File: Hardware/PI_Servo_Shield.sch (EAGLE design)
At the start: 58 parts, among them J1 RASPBERRYPI-40-PIN-GPIO, J19 QWIIC, J20 USB C, J21 Serial, U1 PCA9685, U2 PCA9306, U3 CH340C

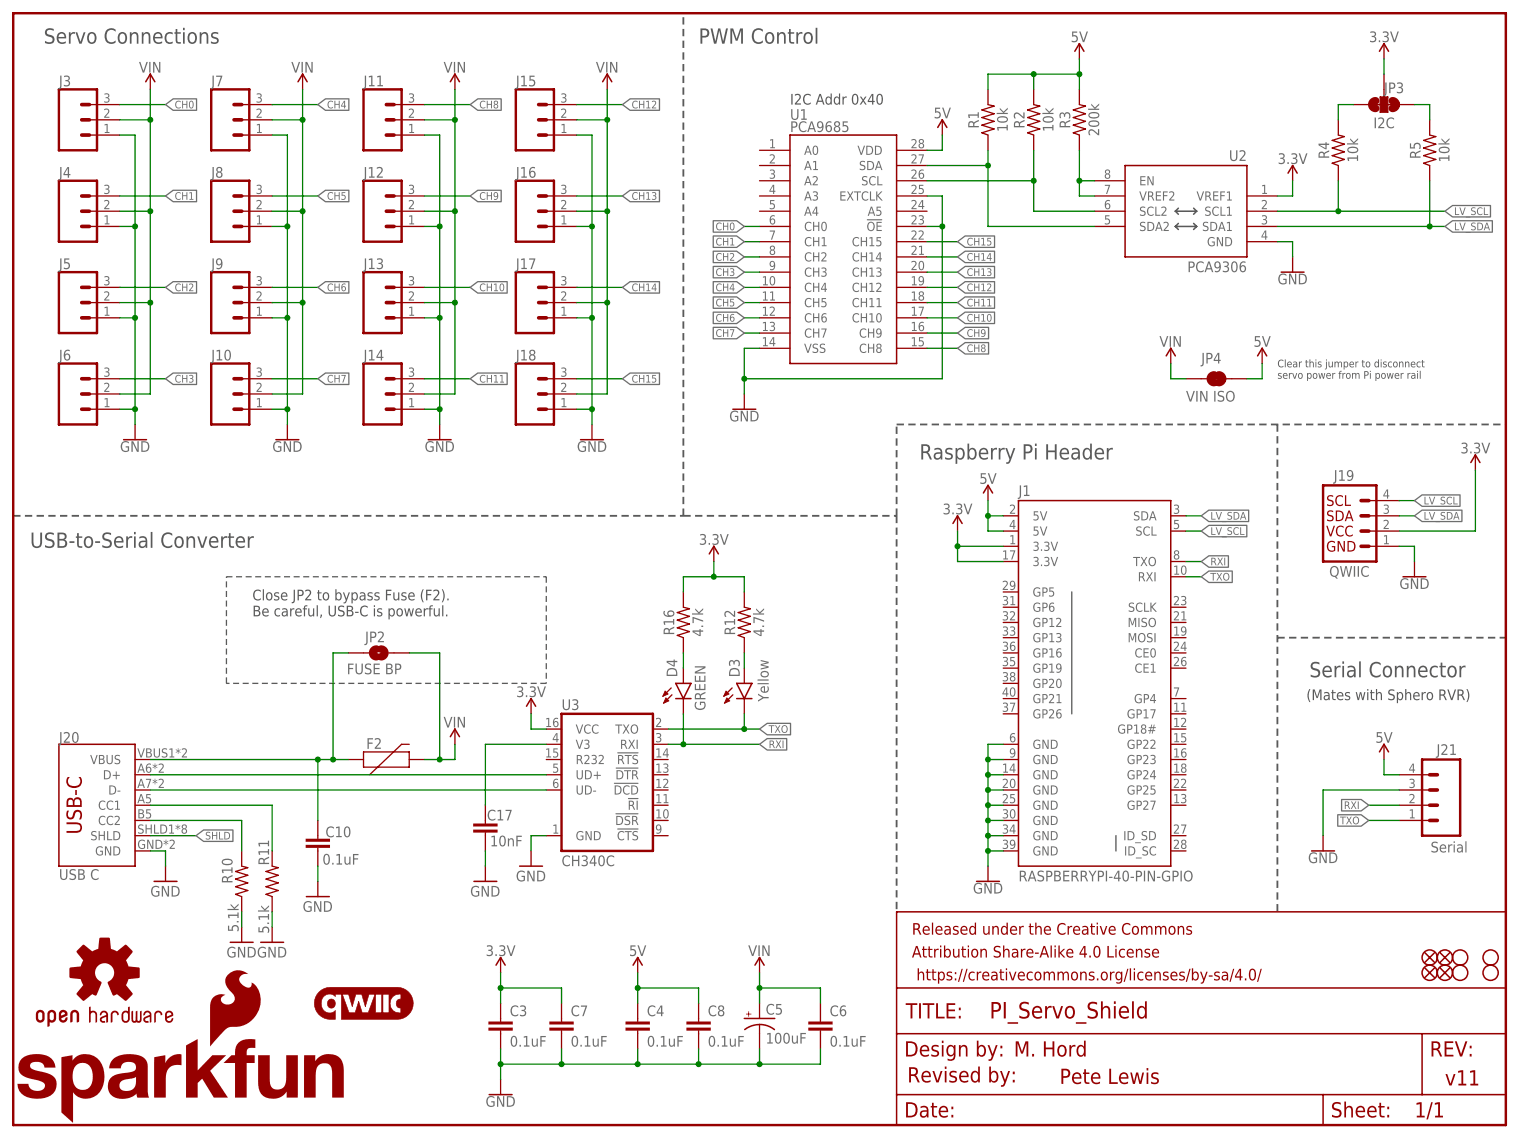
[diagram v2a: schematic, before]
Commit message: post checklist changes - silk and testpoints
-silk outlines up to 8 mil on a few.
-testpoints
-RX/TX LED colors corrected
-some PROD_ID stuff fixed.
-text note in sch for i2c jumper
-voltage warning for > +5V RVR input damaging pi.
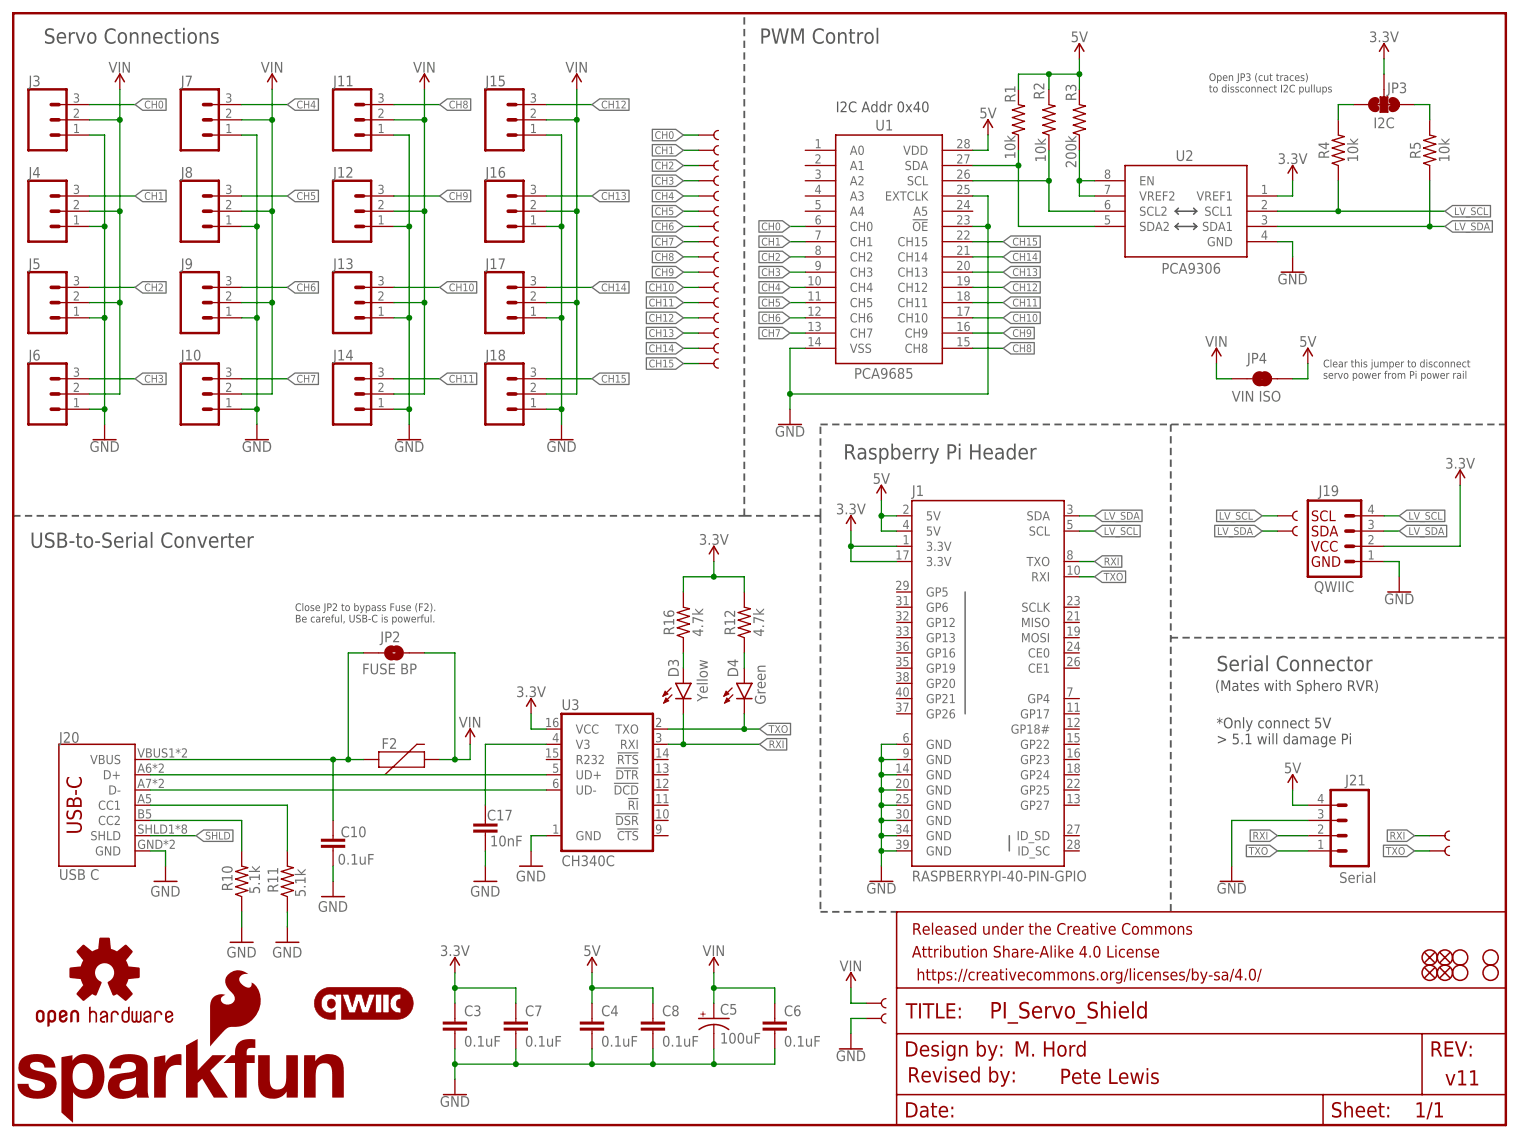
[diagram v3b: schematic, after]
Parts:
- added TP0, TP1, TP10, TP11, TP12, TP13, TP14, TP15, TP16, TP17, TP2, TP20, TP21, TP3, TP4, TP5, TP6, TP7, TP8, TP9: TEST-POINT3X4, SparkFun-Connectors:TEST-POINT3X4
- added TP18, TP19: TEST-POINTTP_15TH_THRU, SparkFun-Connectors:TEST-POINTTP_15TH_THRU
- C3, C4, C6, C7, C8: device SparkFun-Capacitors:0.1UF-0603-25V-5% -> SparkFun-Capacitors:0.1UF-0603-25V-(+80/-20%)
- D3: device SparkFun-LED:LED-YELLOW_HIDDENSILK -> SparkFun-LED:LED-GREEN_HIDDENSILK
- D4: device SparkFun-LED:LED-GREENLILYPAD -> SparkFun-LED:LED-YELLOW_HIDDENSILK
- J20: device USB-C:USB_C16PIN -> SparkFun-Connectors:USB_C16PIN
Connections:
- removed net N$12: D4.A, R16.1
- removed net N$13: D3.A, R12.1
- new net N$6: D3.A, R16.1
- new net N$7: D4.A, R12.1
- net CH0: now also TP0.1
- net CH1: now also TP1.1
- net CH10: now also TP10.1
- net CH11: now also TP11.1
- net CH12: now also TP12.1
- net CH13: now also TP13.1
- net CH14: now also TP14.1
- net CH15: now also TP15.1
- net CH2: now also TP2.1
- net CH3: now also TP3.1
- net CH4: now also TP4.1
- net CH5: now also TP5.1
- net CH6: now also TP6.1
- net CH7: now also TP7.1
- net CH8: now also TP8.1
- net CH9: now also TP9.1
- net GND: now also TP17.1
- net LV_SCL: now also TP18.1
- net LV_SDA: now also TP19.1
- net RXI: now also D3.C, TP20.1; no longer D4.C
- net TXO: now also D4.C, TP21.1; no longer D3.C
- net VIN: now also TP16.1
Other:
- note added: "*Only connect 5V > 5.1 will damage Pi"
- note added: "Green"
- note added: "Open JP3 (cut traces) to dissconnect I2C pullups"
- moved on the sheet: C10, C3, C4, C5, C6, C7, C8, D3, D4, F2, J1, J10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

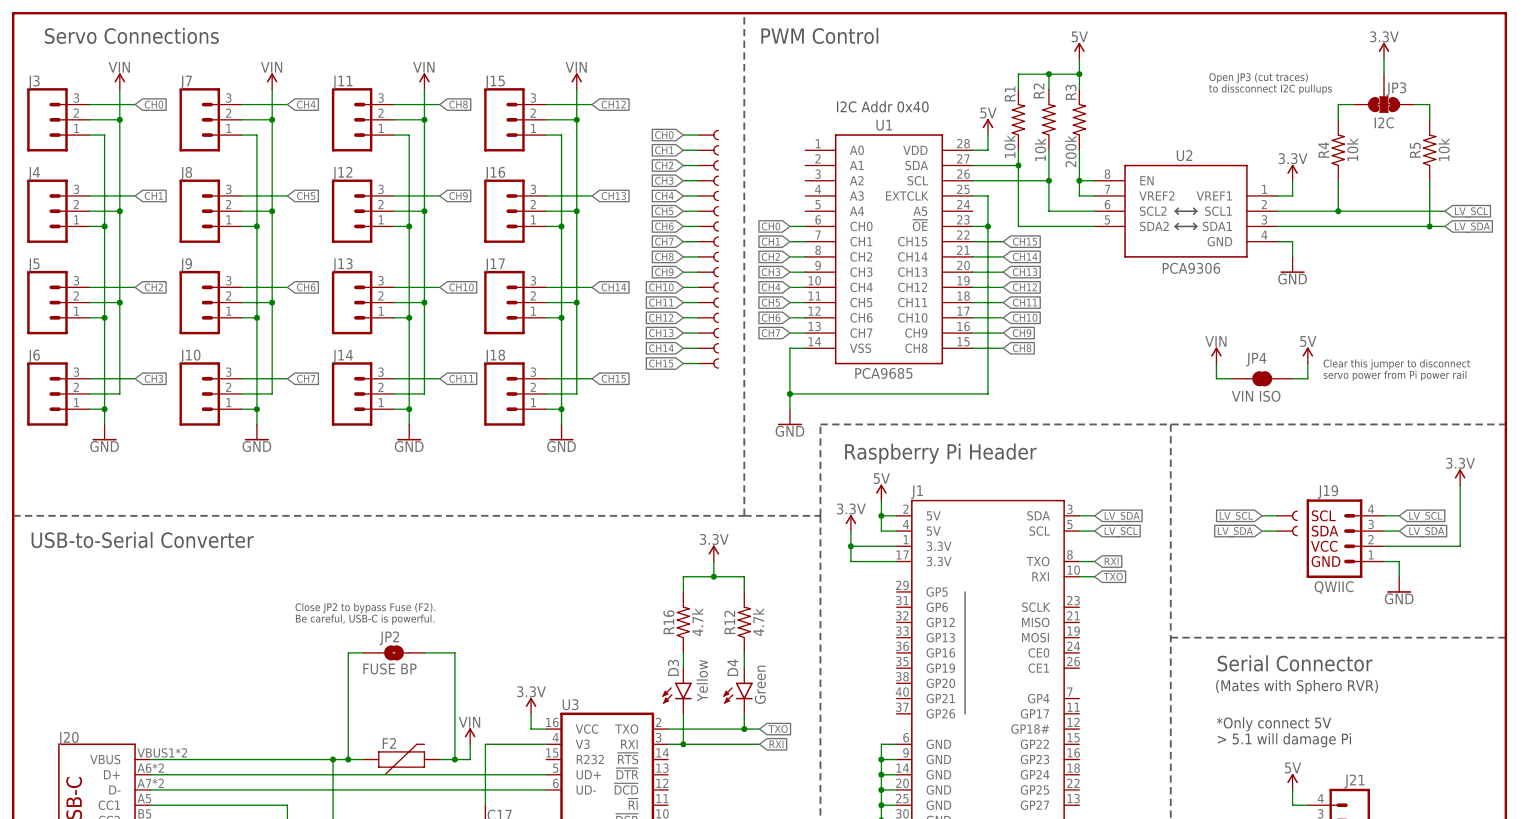
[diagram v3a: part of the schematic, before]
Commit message: post double check stuff - moved from PCA9306 to transistors
-PCA level shifter is EOL, moved to transistor conversion.
-added VCC range note in SCH
-fixed a trace off of PCA PWM chip
-PROD_ID fixes on LEDs
-moved measure to show units
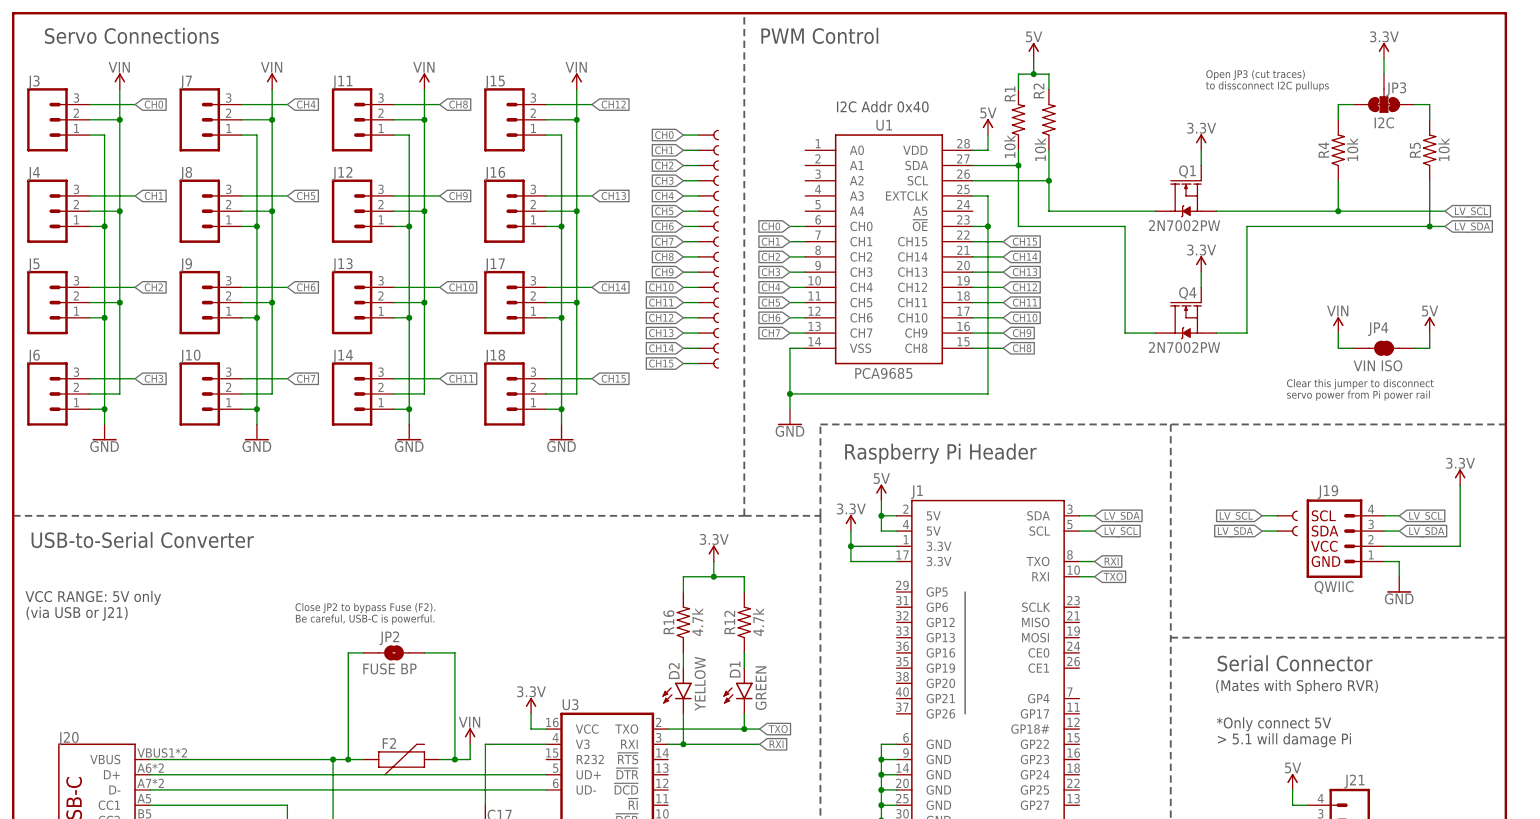
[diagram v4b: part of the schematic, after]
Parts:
- removed D3: Yellow, SparkFun-LED:LED-GREEN_HIDDENSILK
- removed D4: GREEN, SparkFun-LED:LED-YELLOW_HIDDENSILK
- removed R3: 200k, SparkFun-Resistors:200KOHM-0603-1/10W-1%
- removed U2: PCA9306, SparkFun-IC-Comms:PCA9306
- added D1: GREEN, SparkFun-LED:LED-GREEN_HIDDENSILK
- added D2: YELLOW, SparkFun-LED:LED-YELLOW_HIDDENSILK
- added Q1, Q4: 2N7002PW, SparkFun-DiscreteSemi:MOSFET-NCH-2N7002PW
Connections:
- removed net N$1: R3.1, U2.EN, U2.VREF2
- net 3.3V: now also Q1.G, Q4.G; no longer U2.VREF1
- net 5V: no longer R3.2
- net GND: no longer U2.GND
- net LV_SCL: now also Q1.S; no longer U2.SCL1
- net LV_SDA: now also Q4.S; no longer U2.SDA1
- net N$3: now also Q1.D; no longer U2.SCL2
- net N$4: now also Q4.D; no longer U2.SDA2
- net N$6: now also D2.A; no longer D3.A
- net N$7: now also D1.A; no longer D4.A
- net RXI: now also D2.C; no longer D3.C
- net TXO: now also D1.C; no longer D4.C
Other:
- note added: "VCC RANGE: 5V only (via USB or J21)"
- note removed: "Green"
- moved on the sheet: JP4
